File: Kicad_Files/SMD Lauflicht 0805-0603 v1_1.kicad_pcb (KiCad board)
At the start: 2 copper layers, 40 x 40 mm, 55 parts, among them Q1 BC850, Q2 BC850, SW1 SW_DPDT_x2, U1 NE555, U2 4017, U3 4017

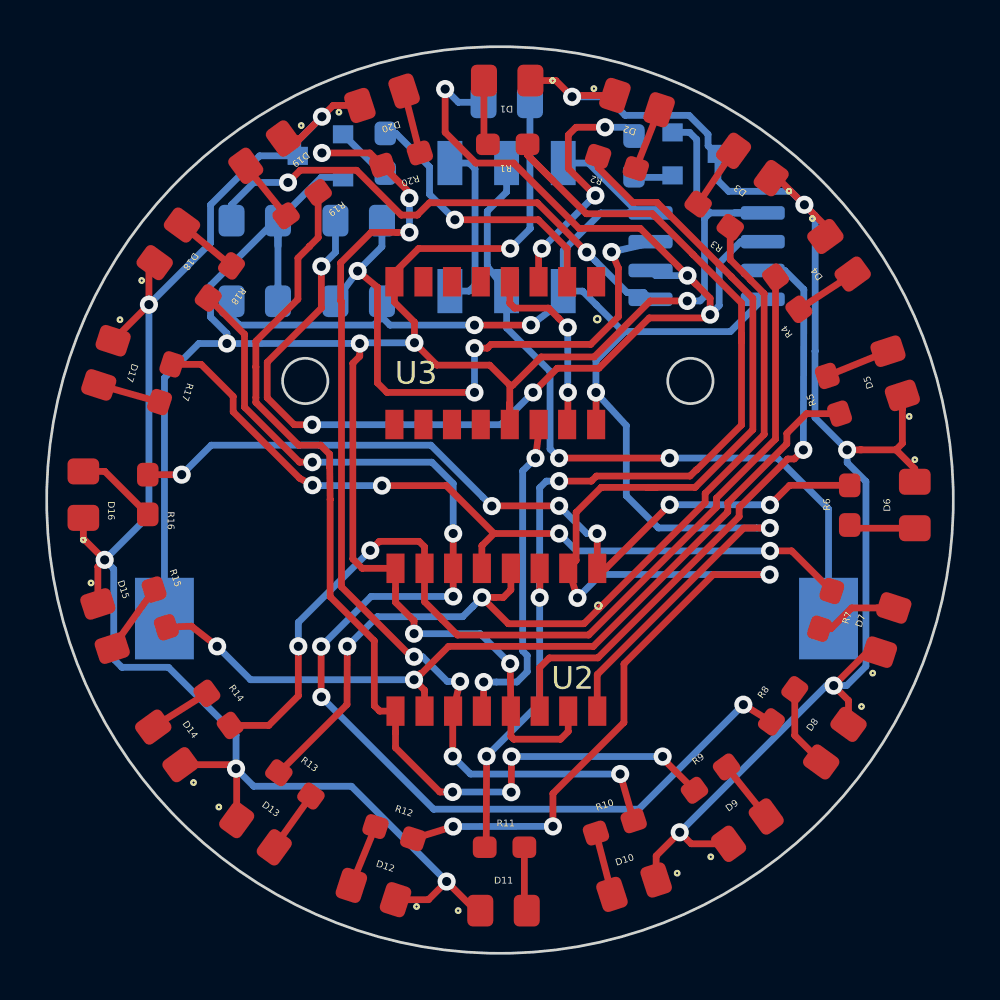
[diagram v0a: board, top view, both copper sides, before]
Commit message: exchanged cr2032 battery holder
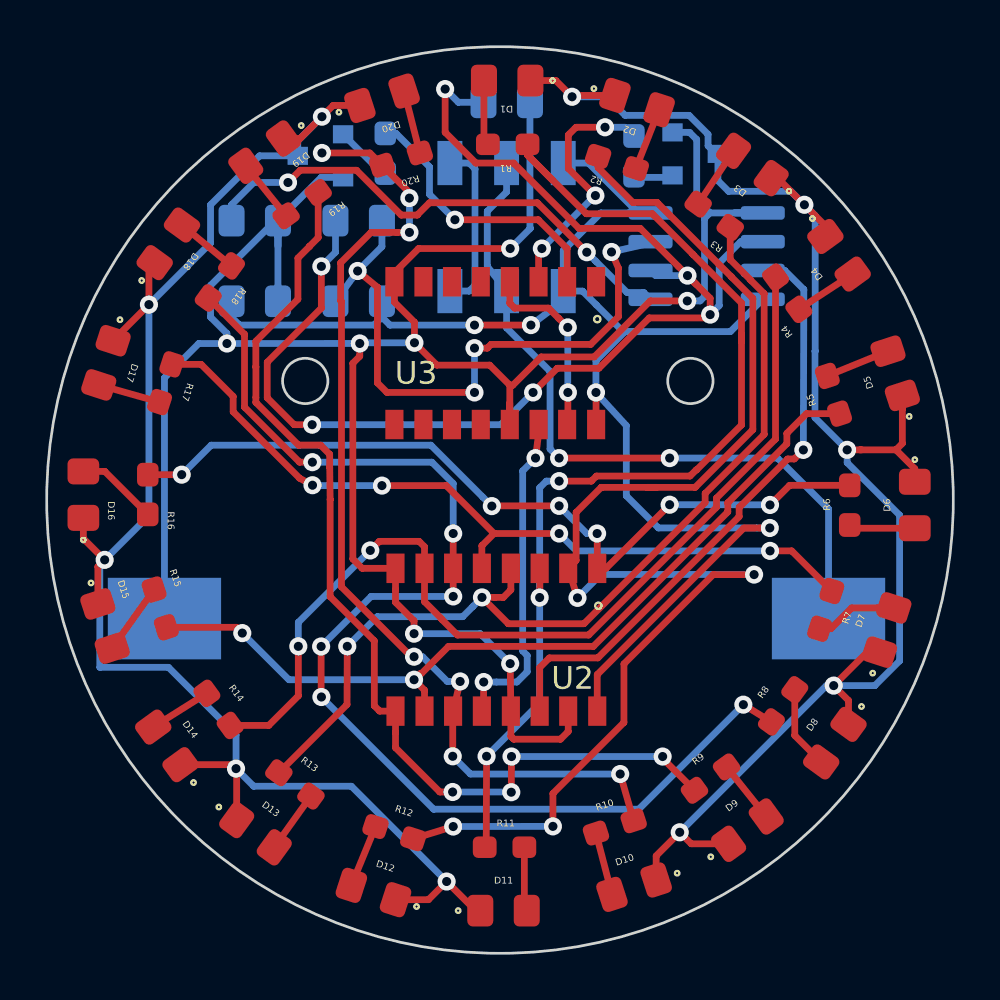
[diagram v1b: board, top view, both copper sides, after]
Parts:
- BT1: footprint Battery:BatteryHolder_Keystone_1060_1x2032 -> Binary Kitchen:BatteryHolder_Keystone_1060_1x2032_HandSoldering
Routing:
- net Net-(D1-Pad1): track 70.4 -> 72.3 mm
- net Net-(R12-Pad1): track 61.2 -> 59.8 mm
- net Net-(D11-Pad1): track 70.6 -> 71.3 mm
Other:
- board text removed: "JLCJLCJLC"
